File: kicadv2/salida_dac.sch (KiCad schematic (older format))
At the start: 22 parts, among them U7 TL064

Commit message: simulaciones y kicad para placa nueva
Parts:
- removed R10, R17, R27: 10K, Resistor_THT:R_Axial_DIN0207_L6.3mm_D2.5mm_P7.62mm_Horizontal, symbol salida_dac-rescue:R-Device
- removed R11: 1K, Resistor_THT:R_Axial_DIN0207_L6.3mm_D2.5mm_P7.62mm_Horizontal, symbol salida_dac-rescue:R-Device
- removed R18: 15K, Resistor_THT:R_Axial_DIN0207_L6.3mm_D2.5mm_P7.62mm_Horizontal, symbol salida_dac-rescue:R-Device
- removed R26: 8.2K, Resistor_THT:R_Axial_DIN0207_L6.3mm_D2.5mm_P7.62mm_Horizontal, symbol salida_dac-rescue:R-Device
- removed RV10, RV12, RV5, RV6, RV8: 1K, Potentiometer_THT:Potentiometer_Bourns_3266Y_Vertical, symbol salida_dac-rescue:R_POT-Device
- removed RV2: R_POT, Potentiometer_THT:Potentiometer_Bourns_3266Y_Vertical, symbol salida_dac-rescue:R_POT-Device
- added D? (x2): 1N4007, Diode_THT:D_DO-41_SOD81_P10.16mm_Horizontal, symbol Diode:1N4007
- added J?: USB_B_Micro, Connector_USB:USB_Mini-B_Wuerth_65100516121_Horizontal, symbol potenciostato-rescue:USB_B_Micro-Connector
- added J?: test_I, Connector_PinHeader_2.54mm:PinHeader_1x01_P2.54mm_Vertical, symbol potenciostato-rescue:Conn_01x01_Female-Connector
- added J?: test_DAC, Connector_PinHeader_2.54mm:PinHeader_1x01_P2.54mm_Vertical, symbol potenciostato-rescue:Conn_01x01_Female-Connector
- added J?: test_V, Connector_PinHeader_2.54mm:PinHeader_1x01_P2.54mm_Vertical, symbol potenciostato-rescue:Conn_01x01_Female-Connector
- added JP?: alimentacion_lpc, Connector_PinHeader_2.54mm:PinHeader_1x02_P2.54mm_Vertical, symbol potenciostato-rescue:Jumper-Device
- added LPC?: LPCXPRESSO_LPC1769, LPC:LPCXPRESSO_LPC1769, symbol potenciostato-rescue:LPCXPRESSO_LPC1769-LPCXPRESSO_LPC1769
- added R? (x2): 5K6, Resistor_THT:R_Axial_DIN0207_L6.3mm_D2.5mm_P7.62mm_Horizontal, symbol salida_dac-rescue:R-Device
- added R?: 4K7, Resistor_THT:R_Axial_DIN0207_L6.3mm_D2.5mm_P7.62mm_Horizontal, symbol salida_dac-rescue:R-Device
- added RV?: 10K, symbol Device:R_POT
- R10, R8: symbol Device:R -> potenciostato-rescue:R-Device
- R13: value 4K7 -> 10K
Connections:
- net labels added: Pin12_U8, Pin13_U8, Pin5_U8, Pin6_U8, VOffset
- net labels removed: DAC1, I_ADC, SW_FILTRO1, SW_FILTRO2, V_ADC
- wire segments 60 -> 74
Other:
- note added: "Amplificador Inversor con ganancia unitaria y offset,\nadapta la señal a 0-3.3V\n(AMP T2)"
- note added: "Amplificador Inversor con ganancia unitaria y offset,\nadapta la señal a 0-3.3V\n(AMP T3)"
- note added: "Amplificador Tension Inversor atenua la señal de dac y\nagrega offset para que la salida tenga valor medio nulo\n(AMP T1)"
- note added: "Buffer, tension de offset para los \namplificadores que adaptan señal"
- note added: "Salida DAC uC de 0 a 3.3V\nSalida módulo amplificador:\n0V = -1V\n1.5V = 0V\n3.3V = +1V"
- note removed: "Amplificador Tension Inversor con selector\nde ganancia y offset\n(AMP I2)"
- note removed: "Amplificador Tension Inversor con selector\nde ganancia y offset\n(AMP T1)"
- note removed: "Amplificador Tension Inversor con selector\nde ganancia y offset\n(AMP T2)"
- note removed: "El offset de este amplificador se regulará para tener valor medio nulo"
- note removed: "El offset de este amplificador se regulará para tener\nvalor medio igual a la mitad del rango del ADC (0 a 3.3V)"
- note removed: "Salida DAC uC de 0 a 3.3V\nSalida módulo amplificador:\n0V = VEE (-5V)\n1.5V = 0V\n3.3V = VCC (5V)"
- note removed: "Salida electrodo: VEE<0<VCC\nEntrada ADC: 0 a 5V (eventualmente 0 a 3.3V)"
- moved on the sheet: R13, R14, R18, R21, R6, R7, R9, U7A, U7B, U7C, U7D, U7E

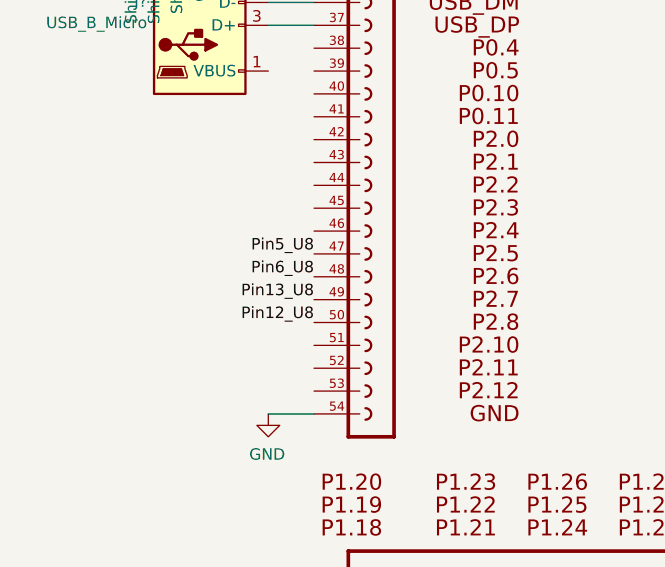
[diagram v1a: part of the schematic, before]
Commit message: se agrega 4316 y ganancia de corriente variable
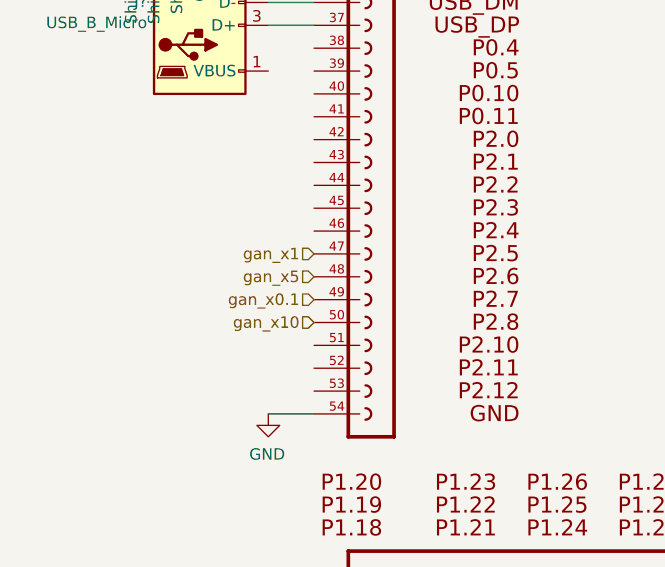
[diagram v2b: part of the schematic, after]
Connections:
- net Pin12_U8 renamed gan_x10
- net Pin13_U8 renamed gan_x0.1
- net Pin5_U8 renamed gan_x1
- net Pin6_U8 renamed gan_x5
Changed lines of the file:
@@
 $Descr A4 11693 8268
 encoding utf-8
-Sheet 2 3
+Sheet 3 2
 Title ""
 Date ""
@@
 	-1   0    0    -1
 $EndComp
-Text Label 1800 3550 2    50   ~ 0
-Pin12_U8
-Text Label 1800 3350 2    50   ~ 0
-Pin6_U8
-Text Label 1800 3250 2    50   ~ 0
-Pin5_U8
-Text Label 1800 3450 2    50   ~ 0
-Pin13_U8
 $Comp
 L potenciostato-rescue:GND-power #PWR?
@@
 Text Notes 2650 6250 0    50   ~ 0
 Buffer, tension de offset para los \namplificadores que adaptan señal
+Text HLabel 1800 3250 0    50   Input ~ 0
+gan_x1
+Text HLabel 1800 3350 0    50   Input ~ 0
+gan_x5
+Text HLabel 1800 3550 0    50   Input ~ 0
+gan_x10
+Text HLabel 1800 3450 0    50   Input ~ 0
+gan_x0.1
 $EndSCHEMATC

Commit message: agregado lo de Hernan y fixeado el kicad pcb
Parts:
- D2, D3: renamed from D?; footprint Diode_THT:D_DO-41_SOD81_P10.16mm_Horizontal -> Diode_SMD:D_1206_3216Metric_Pad1.42x1.75mm_HandSolder
- J7, J8: renamed from J?; footprint Connector_PinHeader_2.54mm:PinHeader_1x01_P2.54mm_Vertical -> Connector_PinHeader_1.00mm:PinHeader_1x01_P1.00mm_Vertical
- LPC1: renamed from LPC?; footprint LPC:LPCXPRESSO_LPC1769 -> kicadv2:LPCXPRESSO_LPC1769
- R1, R10, R13, R16, R4, R8, R9: footprint Resistor_THT:R_Axial_DIN0207_L6.3mm_D2.5mm_P7.62mm_Horizontal -> Resistor_SMD:R_1206_3216Metric_Pad1.30x1.75mm_HandSolder
- R16, R17, R19: renamed from R?; footprint Resistor_THT:R_Axial_DIN0207_L6.3mm_D2.5mm_P7.62mm_Horizontal -> Resistor_SMD:R_1206_3216Metric_Pad1.30x1.75mm_HandSolder
- R2: footprint Resistor_THT:R_Axial_DIN0207_L6.3mm_D2.5mm_P10.16mm_Horizontal -> Resistor_SMD:R_1206_3216Metric_Pad1.30x1.75mm_HandSolder
- RV1: renamed from RV?; footprint (none) -> Potentiometer_THT:Potentiometer_Bourns_3296W_Vertical
- gave numbers to parts that had none: 3

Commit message: hecho esquematico en base a simulacion
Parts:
- removed D2, D3: 1N4007, Diode_SMD:D_1206_3216Metric_Pad1.42x1.75mm_HandSolder, symbol Diode:1N4007
- added R20, R22, R23: 10K, Resistor_SMD:R_1206_3216Metric_Pad1.30x1.75mm_HandSolder, symbol salida_dac-rescue:R-Device
- added U9: TL082, Package_DIP:DIP-8_W7.62mm_LongPads, symbol Amplifier_Operational:TL082
- R10, R16: value 1K -> 10K
- R16, R8: value 5K6 -> 10K
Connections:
- net +5V: now also U9.8 (V+); no longer R16.2
- net -5V: now also U9.4 (V-)
- net GND: now also U7.3 (+), R22.2, R23.2
- net VOffset: now also R16.2, U9.1, U9.2 (-); no longer R2.2, U7.13 (-), U7.14
- net at R1.1, R8.2, U7.2 (-): now also R2.1
- net at R4.1, U7.9 (-): now also R22.1; no longer R9.1
- net at J8.1 (Pin_1), LPC1.16, U7.7: now also R13.1; no longer R13.2
- net at R10.2, U7.5 (+): now also R16.1
- net at R8.2, U7.10 (+): now also R9.1
- net at U7.12 (+): now also U7.13 (-), U7.14; no longer RV1.2
- net at R16.1: now also R20.2, U9.5 (+); no longer R17.2
- net 3V3: now reaches LPC1.28
- net 3V3: now also R17.2
- new net: R13.2, R23.1, U7.6 (-)
- new net: RV1.2, U9.3 (+)
- new net -VOffset: R2.2, R20.1, U9.6 (-), U9.7
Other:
- note added: "Amplificador Inversor con ganancia unitaria y offset,\nadapta la señal a 0-3.3V\n(AMP I2)"
- note added: "Amplificador No Inversor con ganancia unitaria y VOffset,\nadapta la señal a 0-3.3V\n(AMP T2)"
- note added: "Amplificador Tension Inversor de ganancia unitaria (-1)\nla señal de dac y agrega -VOffset para que la salida\ntenga valor medio nulo\n(AMP T1)"
- note added: "Buffer, tension de offset + y - para los \namplificadores que adaptan señal"
- note added: "Salida DAC uC de 0 a 3.3V\nSalida módulo amplificador:\n0V = -1.5V\n1.5V = 0V\n3.3V = +1.5V"
- note removed: "Amplificador Inversor con ganancia unitaria y offset,\nadapta la señal a 0-3.3V\n(AMP T2)"
- note removed: "Amplificador Inversor con ganancia unitaria y offset,\nadapta la señal a 0-3.3V\n(AMP T3)"
- note removed: "Amplificador Tension Inversor atenua la señal de dac y\nagrega offset para que la salida tenga valor medio nulo\n(AMP T1)"
- note removed: "Buffer, tension de offset para los \namplificadores que adaptan señal"
- note removed: "Salida DAC uC de 0 a 3.3V\nSalida módulo amplificador:\n0V = -1V\n1.5V = 0V\n3.3V = +1V"
- moved on the sheet: J2, J7, J8, R13, R14, R17, R18, R19, R6, R7, R8, R9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

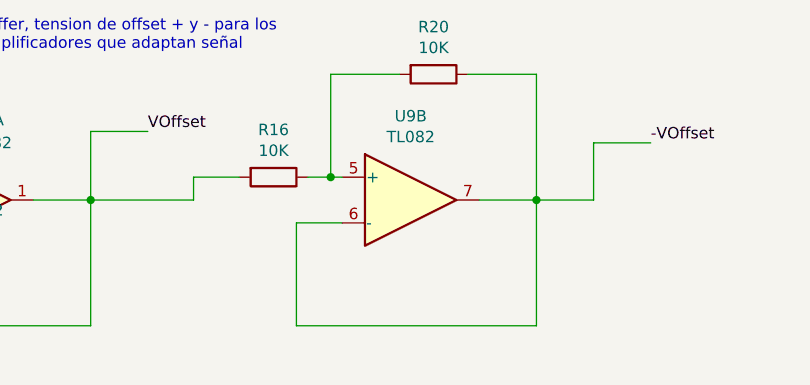
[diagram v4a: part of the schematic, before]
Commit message: pin 7 de u9 a GND
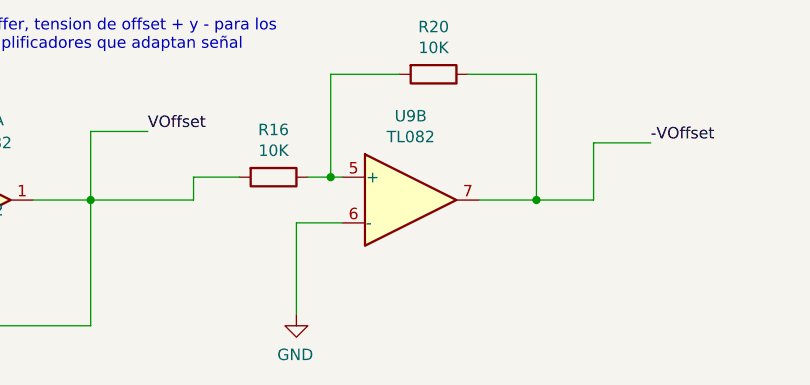
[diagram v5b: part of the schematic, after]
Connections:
- net -VOffset: no longer U9.6 (-)
- net GND: now also U9.6 (-)
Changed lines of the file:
@@
 	3850 6850 3650 6850
-Wire Wire Line
-	3650 7300 4700 7300
 Wire Wire Line
 	4700 6750 4950 6750
@@
 	4950 6750 4950 6500
 Wire Wire Line
-	3650 6850 3650 7300
-Wire Wire Line
-	4700 6750 4700 7300
-Wire Wire Line
 	4950 6500 5200 6500
 Wire Wire Line
@@
 Wire Wire Line
 	4500 3050 6200 3050
+$Comp
+L potenciostato-rescue:GND-power #PWR?
+U 1 1 635F5223
+P 3650 7250
+AR Path="/60147E53/635F5223" Ref="#PWR?"  Part="1"
+AR Path="/6013BA2D/635F5223" Ref="#PWR?"  Part="1"
+F 0 "#PWR?" H 3650 7000 50  0001 C CNN
+F 1 "GND" H 3655 7073 50  0000 C CNN
+F 2 "" H 3650 7250 50  0001 C CNN
+F 3 "" H 3650 7250 50  0001 C CNN
+	1    3650 7250
+	-1   0    0    -1
+$EndComp
+Wire Wire Line
+	3650 6850 3650 7250
 $EndSCHEMATC

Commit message: se agrega version simple fas del pcb
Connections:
- net at U7.12 (+), U7.13 (-): no longer U7.14
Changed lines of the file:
@@
 	10000 6200 10100 6200
-Wire Wire Line
-	10700 6100 10800 6100
-Wire Wire Line
-	10800 6100 10800 5750
-Wire Wire Line
-	10800 5750 10000 5750
-Wire Wire Line
-	10000 5750 10000 6000
-Connection ~ 10000 6000
 Wire Wire Line
 	3850 6650 3800 6650
@@
 P 3650 7250
 AR Path="/60147E53/635F5223" Ref="#PWR?"  Part="1"
-AR Path="/6013BA2D/635F5223" Ref="#PWR?"  Part="1"
-F 0 "#PWR?" H 3650 7000 50  0001 C CNN
+AR Path="/6013BA2D/635F5223" Ref="#PWR0114"  Part="1"
+F 0 "#PWR0114" H 3650 7000 50  0001 C CNN
 F 1 "GND" H 3655 7073 50  0000 C CNN
 F 2 "" H 3650 7250 50  0001 C CNN

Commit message: agregadas vias
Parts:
- J7, J8: footprint Connector_PinHeader_1.00mm:PinHeader_1x01_P1.00mm_Vertical -> Connector_PinHeader_2.54mm:PinHeader_1x01_P2.54mm_Vertical
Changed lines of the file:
@@
 F 0 "J8" H 6450 2850 50  0000 R CNN
 F 1 "test_V" H 6600 2950 50  0000 R CNN
-F 2 "Connector_PinHeader_1.00mm:PinHeader_1x01_P1.00mm_Vertical" H 6500 3050 50  0001 C CNN
+F 2 "Connector_PinHeader_2.54mm:PinHeader_1x01_P2.54mm_Vertical" H 6500 3050 50  0001 C CNN
 F 3 "~" H 6500 3050 50  0001 C CNN
 	1    6500 3050
@@
 F 0 "J7" H 6550 2250 50  0000 R CNN
 F 1 "test_I" H 6650 2350 50  0000 R CNN
-F 2 "Connector_PinHeader_1.00mm:PinHeader_1x01_P1.00mm_Vertical" H 6600 2450 50  0001 C CNN
+F 2 "Connector_PinHeader_2.54mm:PinHeader_1x01_P2.54mm_Vertical" H 6600 2450 50  0001 C CNN
 F 3 "~" H 6600 2450 50  0001 C CNN
 	1    6600 2450

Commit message: puestos USBy trafo OK
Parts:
- J1: footprint Connector_USB:USB_Mini-B_Wuerth_65100516121_Horizontal -> kicadv2:ModuloUSB-Micro
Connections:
- net GND: now also J1.8 (Shield2), J1.9 (Shield3); no longer J1.6 (Shield)
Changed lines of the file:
@@
 F 0 "J1" H 1070 2146 50  0000 R CNN
 F 1 "USB_B_Micro" H 1070 2239 50  0000 R CNN
-F 2 "Connector_USB:USB_Mini-B_Wuerth_65100516121_Horizontal" H 1450 2200 50  0001 C CNN
+F 2 "kicadv2:ModuloUSB-Micro" H 1450 2200 50  0001 C CNN
 F 3 "~" H 1450 2200 50  0001 C CNN
 	1    1300 2250
 	1    0    0    1
 $EndComp
-Wire Wire Line
-	750  1700 1200 1700
 $Comp
 L potenciostato-rescue:GND-power #PWR?
@@
 	-1   0    0    -1
 $EndComp
-Wire Wire Line
-	1200 1850 1200 1700
-Connection ~ 1200 1700
-Wire Wire Line
-	1200 1700 1300 1700
 $Comp
 L potenciostato-rescue:LPCXPRESSO_LPC1769-LPCXPRESSO_LPC1769 LPC?
@@
 Wire Wire Line
 	3650 6850 3650 7250
+Wire Wire Line
+	750  1700 1000 1700
+Wire Wire Line
+	1100 1850 1100 1700
+Connection ~ 1100 1700
+Wire Wire Line
+	1000 1850 1000 1700
+Connection ~ 1000 1700
+Wire Wire Line
+	1000 1700 1100 1700
+Wire Wire Line
+	1100 1700 1300 1700
 $EndSCHEMATC
